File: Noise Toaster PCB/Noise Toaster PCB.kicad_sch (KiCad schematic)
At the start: 0 parts

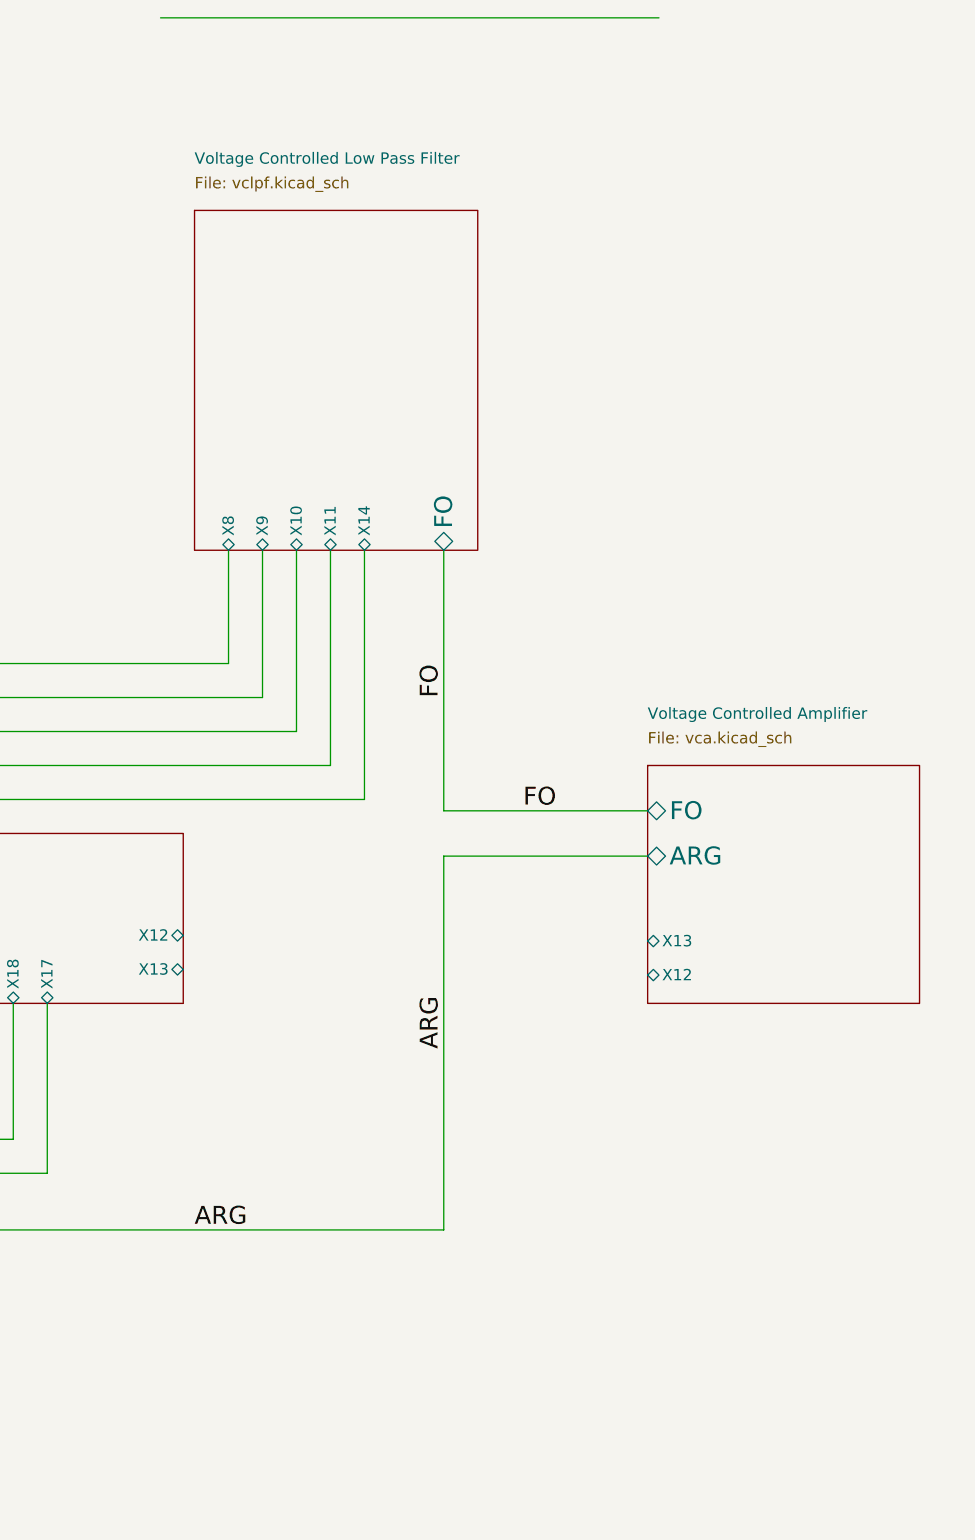
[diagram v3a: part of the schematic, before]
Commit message: color coded wireing and added color legend
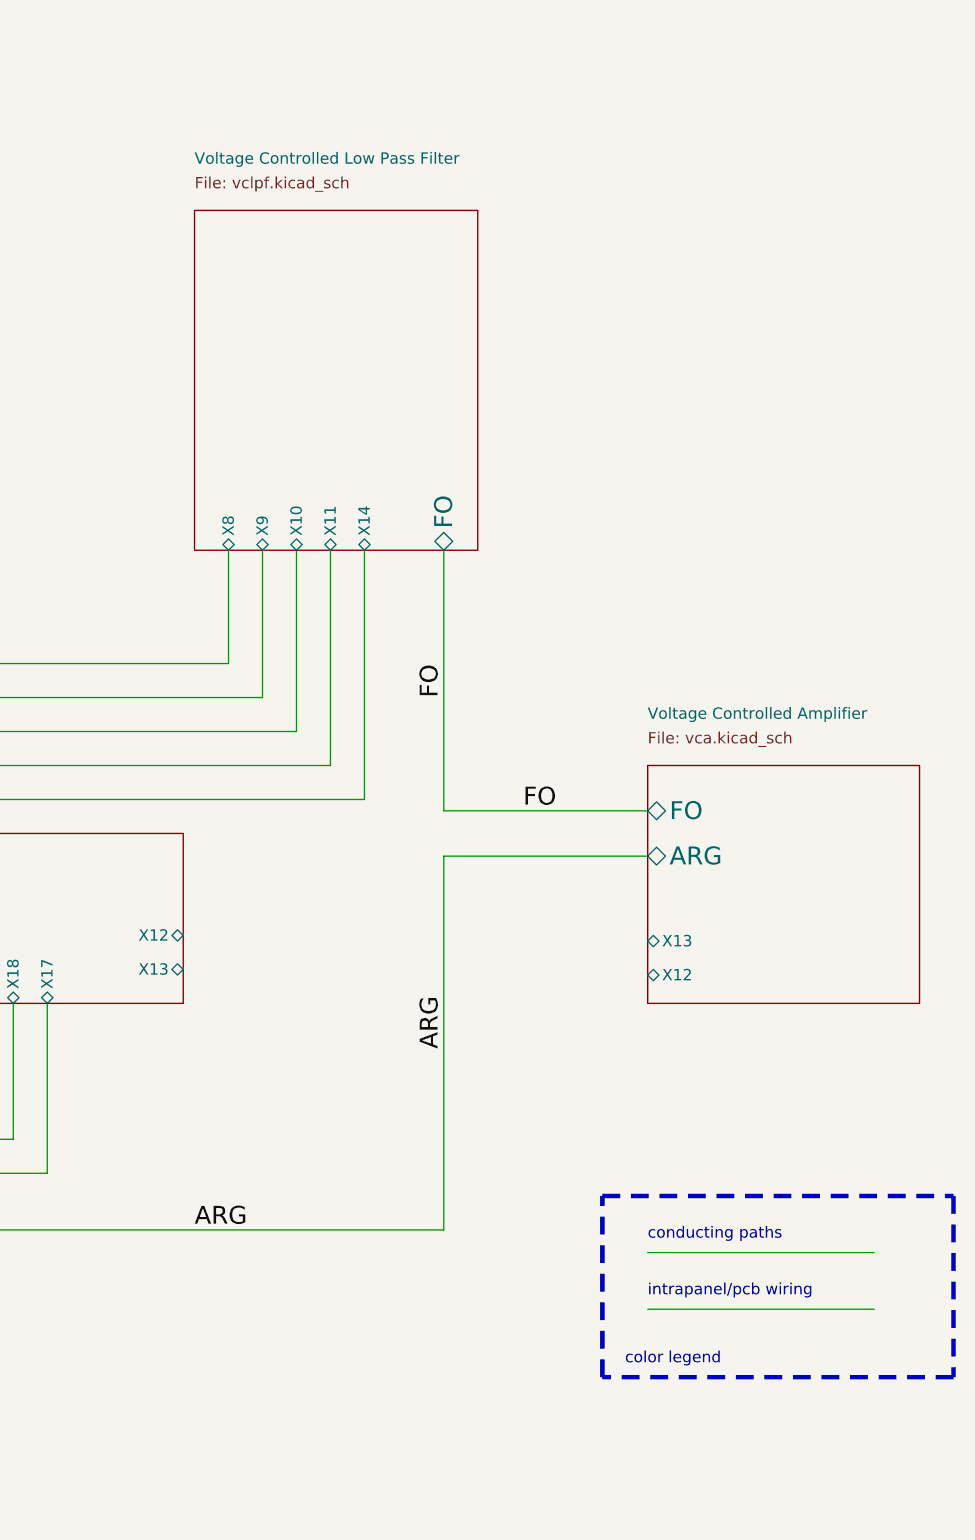
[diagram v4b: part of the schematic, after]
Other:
- note added: "color legend"
- note added: "conducting paths"
- note added: "intrapanel/pcb wiring"
